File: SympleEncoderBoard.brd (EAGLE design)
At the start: 50.8 x 50.8 mm, 31 parts, among them IC1 STM32F446RET6

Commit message: エラー等修正しました。
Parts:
- moved U$1 16.0 mm to (18.9, 40.7)
- moved ERROR 13.2 mm to (38.4, 25.1)
- moved C4 12.5 mm to (34.0, 35.0), flipped to the bottom, turned to 0 degrees
- moved R2 11.2 mm to (30.0, 36.0)
- moved TX 9.22 mm to (38.3, 23.4)
- moved U$3 9.22 mm to (34.0, 36.0)
- moved R1 8.54 mm to (21.7, 30.5), flipped to the bottom, turned to 270 degrees
- moved BOX10P-L1 8.05 mm to (25.4, 47.7)
- moved GYRO 8.00 mm to (10.0, 39.0), turned to 90 degrees
- moved POWER 7.43 mm to (38.4, 16.3)
- moved R4 6.90 mm to (34.0, 37.4), flipped to the bottom, turned to 0 degrees
- moved C6 6.02 mm to (26.1, 30.5), flipped to the bottom
- moved C5 6.00 mm to (19.0, 31.0), flipped to the bottom, turned to 180 degrees
- moved C1 5.74 mm to (18.7, 25.2), flipped to the bottom
- moved R_I1 5.48 mm to (35.4, 22.2), flipped to the bottom, turned to 270 degrees
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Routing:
- net +5V: track 175.9 -> 20.8 mm, vias 0 -> 3
- net +3.3V: track 149.0 -> 21.9 mm, vias 5 -> 4
- net GND: track 74.4 -> 32.6 mm, vias 13 -> 20
- net SWCLK: track 25.0 -> 6.26 mm, vias 3 -> 2
- net SWO: track 23.5 -> 5.63 mm, vias 3 -> 1
- net SWDIO: track 24.4 -> 11.9 mm
- net +12V: track 11.6 -> 0.00 mm
- net ERRORLED: track 20.4 -> 10.7 mm, vias 2 -> 1
- net LED1: track 16.8 -> 8.75 mm, vias 2 -> 1
- net I2C_SDA: track 16.1 -> 24.1 mm, vias 2 -> 4
- net I2C_SCL: track 28.6 -> 36.1 mm, vias 1 -> 4
- net N$1: track 9.08 -> 2.12 mm, vias 2 -> 1
- net SW7: track 20.8 -> 14.5 mm, vias 2 -> 0
- net VCP_RX: track 33.0 -> 26.8 mm, vias 1 -> 4
- net SW3: track 16.1 -> 10.0 mm
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- added copper zone on layer 16, net +12V
- added copper zone on layer 1, net +3.3V
- added copper zone on layer 1, net +5V
- removed copper zone on layer 1, net GND
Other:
- board text removed: "Symple Encoder Board"

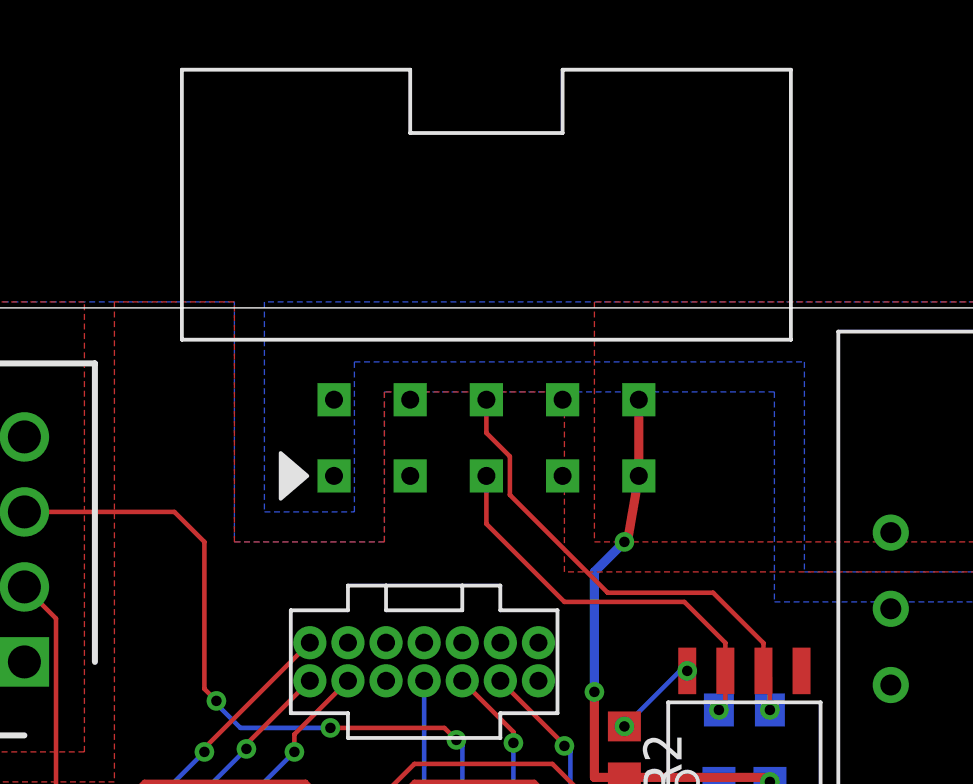
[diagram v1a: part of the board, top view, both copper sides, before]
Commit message: コネクタのホール修正しました
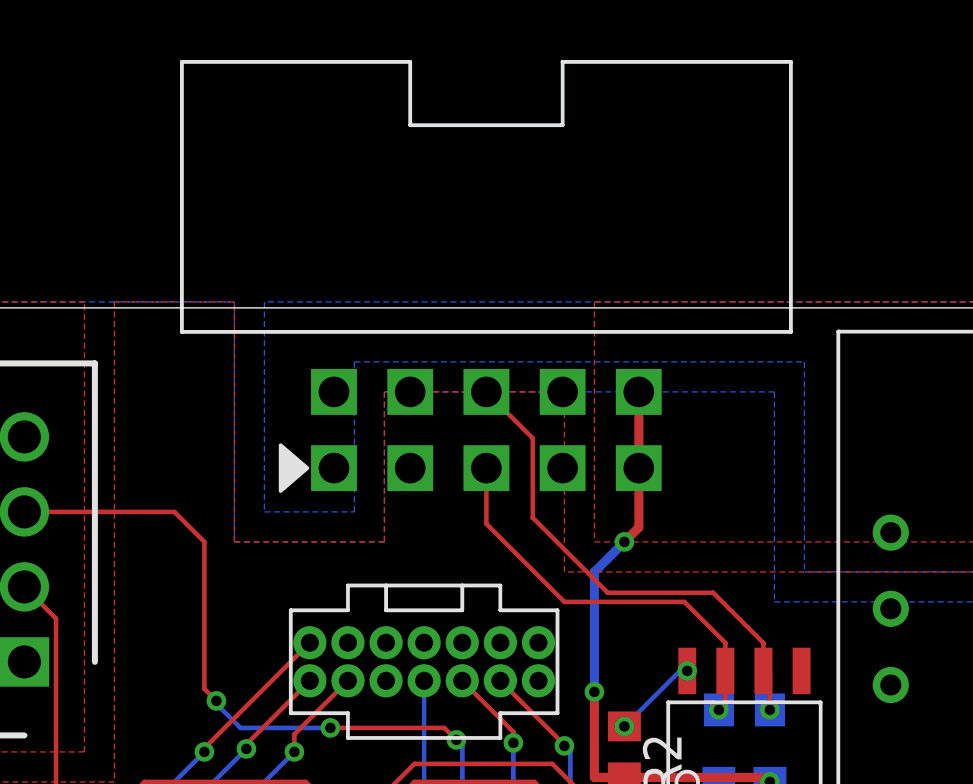
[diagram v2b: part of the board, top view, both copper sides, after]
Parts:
- removed BOX10P-L1: BOX10PBOX10P-L, user_conector:BOX10P-L
- added U$4: BOX10PBOX10P-L, user_conector:BOX10P-L
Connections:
- net +12V: now also U$4.P$1, U$4.P$2; no longer BOX10P-L1.P$1, BOX10P-L1.P$2
- net +5V: now also U$4.P$10, U$4.P$9; no longer BOX10P-L1.P$10, BOX10P-L1.P$9
- net CAN_H: now also U$4.P$5; no longer BOX10P-L1.P$5
- net CAN_L: now also U$4.P$6; no longer BOX10P-L1.P$6
- net GND: now also U$4.P$7, U$4.P$8; no longer BOX10P-L1.P$7, BOX10P-L1.P$8
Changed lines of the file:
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@@
 <attribute name="VALUE" x="37.04" y="17.625" size="1.27" layer="27"/>
 </element>
-<element name="BOX10P-L1" library="user_conector" package="BOX10P-L" value="BOX10PBOX10P-L" x="25.4" y="47.74" smashed="yes" rot="R180"/>
 <element name="C1" library="rcl" library_urn="urn:adsk.eagle:library:334" package="C1608" package3d_urn="urn:adsk.eagle:package:23621/2" value="1μ" x="18.69" y="25.23" smashed="yes" rot="MR270">
 <attribute name="NAME" x="17.055" y="25.865" size="1.27" layer="26" rot="MR270"/>
@@
 <attribute name="VALUE" x="14" y="44" size="1.27" layer="27" rot="R90" align="center"/>
 </element>
+<element name="U$4" library="user_conector" package="BOX10P-L" value="BOX10PBOX10P-L" x="25.4" y="48" smashed="yes" rot="R180"/>
 </elements>
 <signals>
@@
 <contactref element="ENCODER_Y" pad="1"/>
 <contactref element="U$2" pad="P$2"/>
-<contactref element="BOX10P-L1" pad="P$7"/>
-<contactref element="BOX10P-L1" pad="P$8"/>
 <contactref element="U$3" pad="P$2"/>
 <contactref element="C4" pad="2"/>
@@
 <wire x1="23" y1="25" x2="23.68" y2="24.32" width="0.3048" layer="16"/>
 <wire x1="23.68" y1="24.32" x2="23.68" y2="23.68" width="0.3048" layer="16"/>
+<contactref element="U$4" pad="P$7"/>
+<contactref element="U$4" pad="P$8"/>
 </signal>
 <signal name="NRST">
@@
 <contactref element="ENCODER_X" pad="4"/>
 <contactref element="ENCODER_Y" pad="4"/>
-<contactref element="BOX10P-L1" pad="P$10"/>
-<contactref element="BOX10P-L1" pad="P$9"/>
 <contactref element="U$3" pad="P$3"/>
 <contactref element="C4" pad="1"/>
@@
 <wire x1="29" y1="38" x2="29" y2="42" width="0.3048" layer="16"/>
 <via x="30" y="43" extent="1-16" drill="0.35"/>
-<wire x1="30" y1="43" x2="30.12" y2="43.12" width="0.3048" layer="1"/>
-<wire x1="30.12" y1="43.12" x2="30.48" y2="45.2" width="0.3048" layer="1"/>
-<wire x1="30.48" y1="45.2" x2="30.48" y2="47.74" width="0.3048" layer="1"/>
 <polygon width="0.1524" layer="1" thermals="no">
 <vertex x="29" y="51"/>
@@
 <vertex x="51" y="51"/>
 </polygon>
+<contactref element="U$4" pad="P$10"/>
+<contactref element="U$4" pad="P$9"/>
+<wire x1="30.48" y1="48" x2="30.48" y2="45.46" width="0.3048" layer="1"/>
+<wire x1="30.48" y1="45.46" x2="30.48" y2="43.48" width="0.3048" layer="1"/>
+<wire x1="30.48" y1="43.48" x2="30" y2="43" width="0.3048" layer="1"/>
 </signal>
 <signal name="CAN_L">
-<contactref element="BOX10P-L1" pad="P$6"/>
 <contactref element="U$3" pad="P$6"/>
 <contactref element="R4" pad="1"/>
@@
 <wire x1="34.635" y1="39.6282875" x2="32.9584875" y2="41.3048" width="0.1524" layer="1"/>
 <wire x1="32.9584875" y1="41.3048" x2="29.4439125" y2="41.3048" width="0.1524" layer="1"/>
-<wire x1="29.4439125" y1="41.3048" x2="26.1826" y2="44.5661125" width="0.1524" layer="1"/>
-<wire x1="26.1826" y1="44.5661125" x2="26.1826" y2="45.8486875" width="0.1524" layer="1"/>
-<wire x1="25.4" y1="46.6312875" x2="25.4" y2="47.74" width="0.1524" layer="1"/>
-<wire x1="26.1826" y1="45.8486875" x2="25.4" y2="46.6312875" width="0.1524" layer="1"/>
+<contactref element="U$4" pad="P$6"/>
+<wire x1="29.4439125" y1="41.3048" x2="26.9464" y2="43.8023125" width="0.1524" layer="1"/>
+<wire x1="26.9464" y1="46.4536" x2="25.4" y2="48" width="0.1524" layer="1"/>
+<wire x1="26.9464" y1="43.8023125" x2="26.9464" y2="46.4536" width="0.1524" layer="1"/>
 </signal>
 <signal name="CAN_H">
-<contactref element="BOX10P-L1" pad="P$5"/>
 <contactref element="U$3" pad="P$7"/>
 <contactref element="R4" pad="2"/>
@@
 <wire x1="32" y1="41" x2="33.365" y2="39.635" width="0.1524" layer="1"/>
 <wire x1="33.365" y1="39.635" x2="33.365" y2="38.7" width="0.1524" layer="1"/>
-<wire x1="25.4" y1="45.2" x2="25.4" y2="43.6" width="0.1524" layer="1"/>
-<wire x1="25.4" y1="43.6" x2="28" y2="41" width="0.1524" layer="1"/>
+<wire x1="28" y1="41" x2="25.4" y2="43.6" width="0.1524" layer="1"/>
 <wire x1="28" y1="41" x2="32" y2="41" width="0.1524" layer="1"/>
+<contactref element="U$4" pad="P$5"/>
+<wire x1="25.4" y1="43.6" x2="25.4" y2="45.46" width="0.1524" layer="1"/>
 </signal>
 <signal name="+12V">
 <contactref element="U$2" pad="P$1"/>
-<contactref element="BOX10P-L1" pad="P$1"/>
-<contactref element="BOX10P-L1" pad="P$2"/>
 <polygon width="0.1524" layer="16" thermals="no">
 <vertex x="21" y="44"/>
@@
 <vertex x="18" y="44"/>
 </polygon>
+<contactref element="U$4" pad="P$2"/>
+<contactref element="U$4" pad="P$1"/>
 </signal>
 <signal name="N$8">

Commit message: 集合抵抗の値を変えました
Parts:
- R_I1: value 150 -> 1k
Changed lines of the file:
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@@
 <attribute name="VALUE" x="37.04" y="19.675" size="1.27" layer="27"/>
 </element>
-<element name="R_I1" library="user_rcl" package="0603X4RESISTOR" value="150" x="35.42" y="22.24" smashed="yes" rot="MR270">
+<element name="R_I1" library="user_rcl" package="0603X4RESISTOR" value="1k" x="35.42" y="22.24" smashed="yes" rot="MR270">
 <attribute name="NAME" x="34.15" y="22.2125" size="1.27" layer="26" rot="MR270"/>
 <attribute name="VALUE" x="33.96" y="23.2125" size="1.27" layer="28" rot="MR270"/>

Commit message: SDAピンをPC11からPC12に修正した。
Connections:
- net I2C_SDA: now also IC1.53; no longer IC1.52
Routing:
- net GND: vias 20 -> 25
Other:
- board text added: "Symple Encoder Board"
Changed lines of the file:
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@@
 <hole x="2.54" y="48.26" drill="3.5"/>
 <text x="6" y="2" size="2.54" layer="25">KRP</text>
+<text x="33.9" y="6.4" size="1.778" layer="25">Symple
+Encoder
+Board</text>
 </plain>
 <attributes>
@@
 <wire x1="20.46" y1="24.31" x2="19.885" y2="24.885" width="0.3048" layer="16"/>
 <wire x1="19.885" y1="24.885" x2="18.69" y2="26.08" width="0.3048" layer="16"/>
-<wire x1="20" y1="25" x2="23" y2="25" width="0.3048" layer="16"/>
+<wire x1="20" y1="25" x2="21" y2="25" width="0.3048" layer="16"/>
+<wire x1="21" y1="25" x2="22" y2="25" width="0.3048" layer="16"/>
+<wire x1="22" y1="25" x2="23" y2="25" width="0.3048" layer="16"/>
 <wire x1="20" y1="25" x2="19.885" y2="24.885" width="0.3048" layer="16"/>
 <wire x1="18.69" y1="26.08" x2="18.69" y2="28.69" width="0.3048" layer="16"/>
 <wire x1="19.85" y1="29.85" x2="19.85" y2="31" width="0.3048" layer="16"/>
-<wire x1="18.69" y1="28.69" x2="19.85" y2="29.85" width="0.3048" layer="16"/>
+<wire x1="18.69" y1="28.69" x2="19" y2="29" width="0.3048" layer="16"/>
+<wire x1="19" y1="29" x2="19.85" y2="29.85" width="0.3048" layer="16"/>
 <wire x1="26.1" y1="29.65" x2="21.68" y2="29.65" width="0.3048" layer="16"/>
 <wire x1="21.68" y1="29.65" x2="21.67" y2="29.64" width="0.3048" layer="16"/>
@@
 <contactref element="U$4" pad="P$7"/>
 <contactref element="U$4" pad="P$8"/>
+<via x="19" y="29" extent="1-16" drill="0.35"/>
+<via x="20" y="25" extent="1-16" drill="0.35"/>
+<via x="21" y="25" extent="1-16" drill="0.35"/>
+<via x="22" y="25" extent="1-16" drill="0.35"/>
+<via x="23" y="25" extent="1-16" drill="0.35"/>
 </signal>
 <signal name="NRST">
@@
 </signal>
 <signal name="I2C_SDA">
-<contactref element="IC1" pad="52"/>
 <contactref element="GYRO" pad="3"/>
-<wire x1="24.75" y1="32.918" x2="24.75" y2="34.25" width="0.1524" layer="1"/>
-<wire x1="24.75" y1="34.25" x2="24.6" y2="34.4" width="0.1524" layer="1"/>
-<via x="24.6" y="34.4" extent="1-16" drill="0.35"/>
-<wire x1="24.6" y1="34.4" x2="24.6" y2="36.2" width="0.1524" layer="16"/>
-<wire x1="24.6" y1="36.2" x2="24.4" y2="36.4" width="0.1524" layer="16"/>
-<via x="24.4" y="36.4" extent="1-16" drill="0.35"/>
-<wire x1="24.4" y1="36.4" x2="24" y2="36.8" width="0.1524" layer="1"/>
-<wire x1="24" y1="36.8" x2="20.2" y2="36.8" width="0.1524" layer="1"/>
+<via x="24.5" y="34.4" extent="1-16" drill="0.35"/>
+<wire x1="23.9" y1="36.5" x2="24.5" y2="35.9" width="0.1524" layer="16"/>
+<wire x1="24.5" y1="35.9" x2="24.5" y2="34.4" width="0.1524" layer="16"/>
+<via x="23.9" y="36.5" extent="1-16" drill="0.35"/>
+<wire x1="23.9" y1="36.5" x2="23.6" y2="36.8" width="0.1524" layer="1"/>
+<wire x1="23.6" y1="36.8" x2="20.2" y2="36.8" width="0.1524" layer="1"/>
 <via x="20.2" y="36.8" extent="1-16" drill="0.35"/>
 <wire x1="20.2" y1="36.8" x2="17.2" y2="36.8" width="0.1524" layer="16"/>
@@
 <wire x1="16" y1="43" x2="15" y2="44" width="0.1524" layer="1"/>
 <wire x1="15" y1="44" x2="10" y2="44" width="0.1524" layer="1"/>
+<contactref element="IC1" pad="53"/>
+<wire x1="24.5" y1="34.4" x2="24.25" y2="34.15" width="0.1524" layer="1"/>
+<wire x1="24.25" y1="34.15" x2="24.25" y2="32.918" width="0.1524" layer="1"/>
 </signal>
 <signal name="SWCLK">
@@
 <contactref element="IC1" pad="28"/>
 <contactref element="S1" pad="12"/>
-<wire x1="24.1286" y1="21.3206" x2="24.25" y2="21.442" width="0.1524" layer="1"/>
-<wire x1="20.6" y1="15.99" x2="24.1286" y2="19.5186" width="0.1524" layer="1"/>
-<wire x1="24.1286" y1="19.5186" x2="24.1286" y2="21.3206" width="0.1524" layer="1"/>
+<wire x1="24.25" y1="19.64" x2="24.25" y2="21.442" width="0.1524" layer="1"/>
+<wire x1="20.6" y1="15.99" x2="24.25" y2="19.64" width="0.1524" layer="1"/>
 </signal>
 <signal name="SW5">
@@
 <via x="32.095" y="38.7" extent="1-16" drill="0.35"/>
 </signal>
+<signal name="N$9">
+<via x="18" y="32" extent="1-16" drill="0.35"/>
+</signal>
+<signal name="N$10">
+<via x="18" y="30" extent="1-16" drill="0.35"/>
+</signal>
+<signal name="N$11">
+<via x="19" y="30" extent="1-16" drill="0.35"/>
+</signal>
+<signal name="N$12">
+<via x="18" y="29" extent="1-16" drill="0.35"/>
+</signal>
+<signal name="N$13">
+<via x="20" y="29" extent="1-16" drill="0.35"/>
+</signal>
+<signal name="N$14">
+<via x="18" y="28" extent="1-16" drill="0.35"/>
+</signal>
+<signal name="N$15">
+<via x="20" y="28" extent="1-16" drill="0.35"/>
+</signal>
+<signal name="N$16">
+<via x="21" y="28" extent="1-16" drill="0.35"/>
+</signal>
+<signal name="N$17">
+<via x="22" y="28" extent="1-16" drill="0.35"/>
+</signal>
+<signal name="N$18">
+<via x="23" y="28" extent="1-16" drill="0.35"/>
+</signal>
+<signal name="N$19">
+<via x="24" y="28" extent="1-16" drill="0.35"/>
+</signal>
+<signal name="N$20">
+<via x="24" y="29" extent="1-16" drill="0.35"/>
+</signal>
+<signal name="N$21">
+<via x="23" y="29" extent="1-16" drill="0.35"/>
+</signal>
+<signal name="N$22">
+<via x="20" y="27" extent="1-16" drill="0.35"/>
+</signal>
+<signal name="N$23">
+<via x="21" y="27" extent="1-16" drill="0.35"/>
+</signal>
+<signal name="N$24">
+<via x="22" y="27" extent="1-16" drill="0.35"/>
+</signal>
+<signal name="N$25">
+<via x="23" y="27" extent="1-16" drill="0.35"/>
+</signal>
+<signal name="N$26">
+<via x="24" y="27" extent="1-16" drill="0.35"/>
+</signal>
+<signal name="N$27">
+<via x="25" y="27" extent="1-16" drill="0.35"/>
+</signal>
+<signal name="N$28">
+<via x="26" y="26" extent="1-16" drill="0.35"/>
+</signal>
+<signal name="N$29">
+<via x="27" y="26" extent="1-16" drill="0.35"/>
+</signal>
+<signal name="N$30">
+<via x="25" y="26" extent="1-16" drill="0.35"/>
+</signal>
+<signal name="N$31">
+<via x="24" y="26" extent="1-16" drill="0.35"/>
+</signal>
+<signal name="N$32">
+<via x="23" y="26" extent="1-16" drill="0.35"/>
+</signal>
+<signal name="N$33">
+<via x="22" y="26" extent="1-16" drill="0.35"/>
+</signal>
+<signal name="N$34">
+<via x="21" y="26" extent="1-16" drill="0.35"/>
+</signal>
+<signal name="N$35">
+<via x="20" y="26" extent="1-16" drill="0.35"/>
+</signal>
+<signal name="N$36">
+<via x="24" y="25" extent="1-16" drill="0.35"/>
+</signal>
+<signal name="N$37">
+<via x="25" y="25" extent="1-16" drill="0.35"/>
+</signal>
+<signal name="N$38">
+<via x="26" y="25" extent="1-16" drill="0.35"/>
+</signal>
+<signal name="N$39">
+<via x="27" y="25" extent="1-16" drill="0.35"/>
+</signal>
+<signal name="N$40">
+<via x="27" y="24" extent="1-16" drill="0.35"/>
+</signal>
+<signal name="N$41">
+<via x="27" y="23" extent="1-16" drill="0.35"/>
+</signal>
+<signal name="N$42">
+<via x="18" y="23" extent="1-16" drill="0.35"/>
+</signal>
+<signal name="N$43">
+<via x="23" y="31" extent="1-16" drill="0.35"/>
+</signal>
+<signal name="N$44">
+<via x="24" y="31" extent="1-16" drill="0.35"/>
+</signal>
+<signal name="N$45">
+<via x="25" y="31" extent="1-16" drill="0.35"/>
+</signal>
 </signals>
 <mfgpreviewcolors>
@@
 </drawing>
 <compatibility>
+<note version="6.3" minversion="6.2.2" severity="warning">
+Since Version 6.2.2 text objects can contain more than one line,
+which will not be processed correctly with this version.
+</note>
 <note version="8.2" severity="warning">
 Since Version 8.2, EAGLE supports online libraries. The ids
